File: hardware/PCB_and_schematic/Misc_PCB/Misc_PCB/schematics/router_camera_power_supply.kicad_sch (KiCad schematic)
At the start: 15 parts, among them J1 DC_POWER_SUPPLY, J10 DC_POWER_SUPPLY, J9 DC_POWER_SUPPLY, U2 MC34063AP

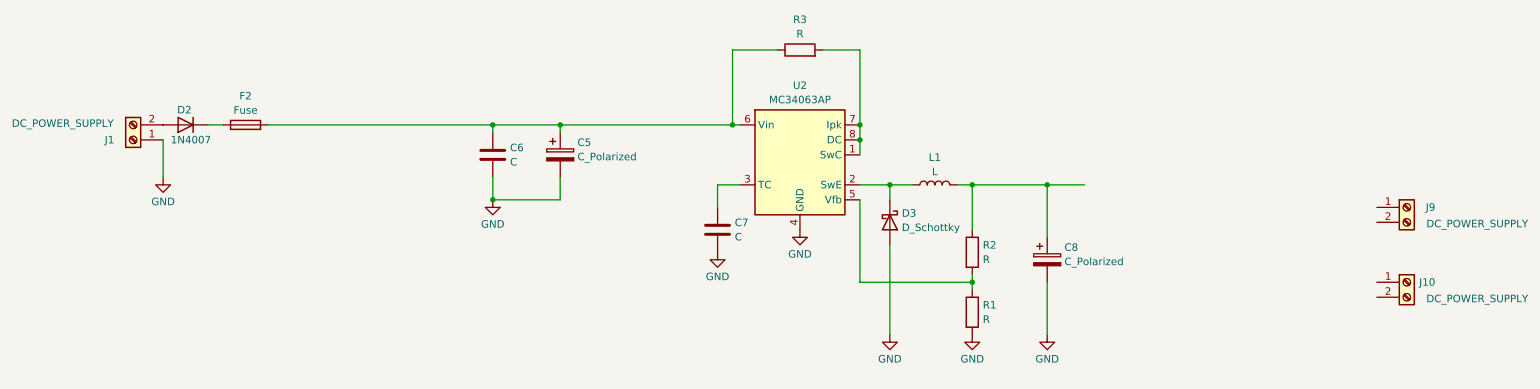
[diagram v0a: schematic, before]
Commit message: Add SD card switcher circuit, some changes in pcb and schematic
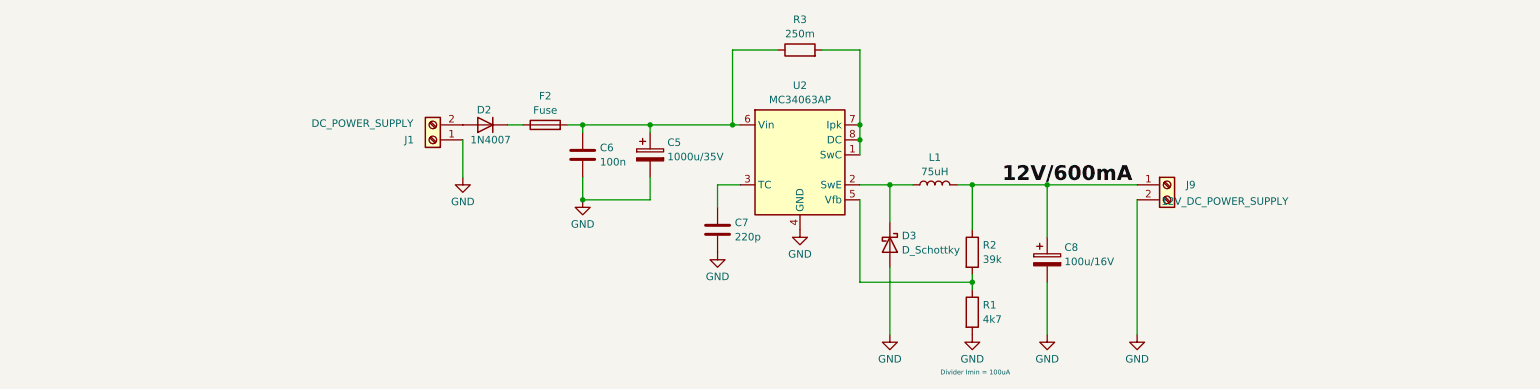
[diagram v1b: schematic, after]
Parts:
- removed J10: DC_POWER_SUPPLY, TerminalBlock:TerminalBlock_Altech_AK300-2_P5.00mm, symbol Connector:Screw_Terminal_01x02
- C5: value C_Polarized -> 1000u/35V
- C6: value C -> 100n
- C7: value C -> 220p
- C8: value C_Polarized -> 100u/16V
- J9: value DC_POWER_SUPPLY -> 12V_DC_POWER_SUPPLY
- L1: value L -> 75uH
- R1: value R -> 4k7
- R2: value R -> 39k
- R3: value R -> 250m
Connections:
- net GND: now also J9.2 (Pin_2)
- net 12V/600mA: now reaches C8.1, L1.2, R2.1
- net 12V/600mA: now also J9.1 (Pin_1)
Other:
- note added: "Divider Imin = 100uA"
- moved on the sheet: C5, C6, D2, D3, F2, J1, J9
